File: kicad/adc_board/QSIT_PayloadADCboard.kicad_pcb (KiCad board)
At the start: 4 copper layers, 36 x 36 mm, 34 parts, among them J1 Conn_02x05_Odd_Even, J2 Conn_02x05_Odd_Even, J3 Conn_02x05_Odd_Even, U1 MCP3561_4CH, U2 NCP1117-3.3_SOT223

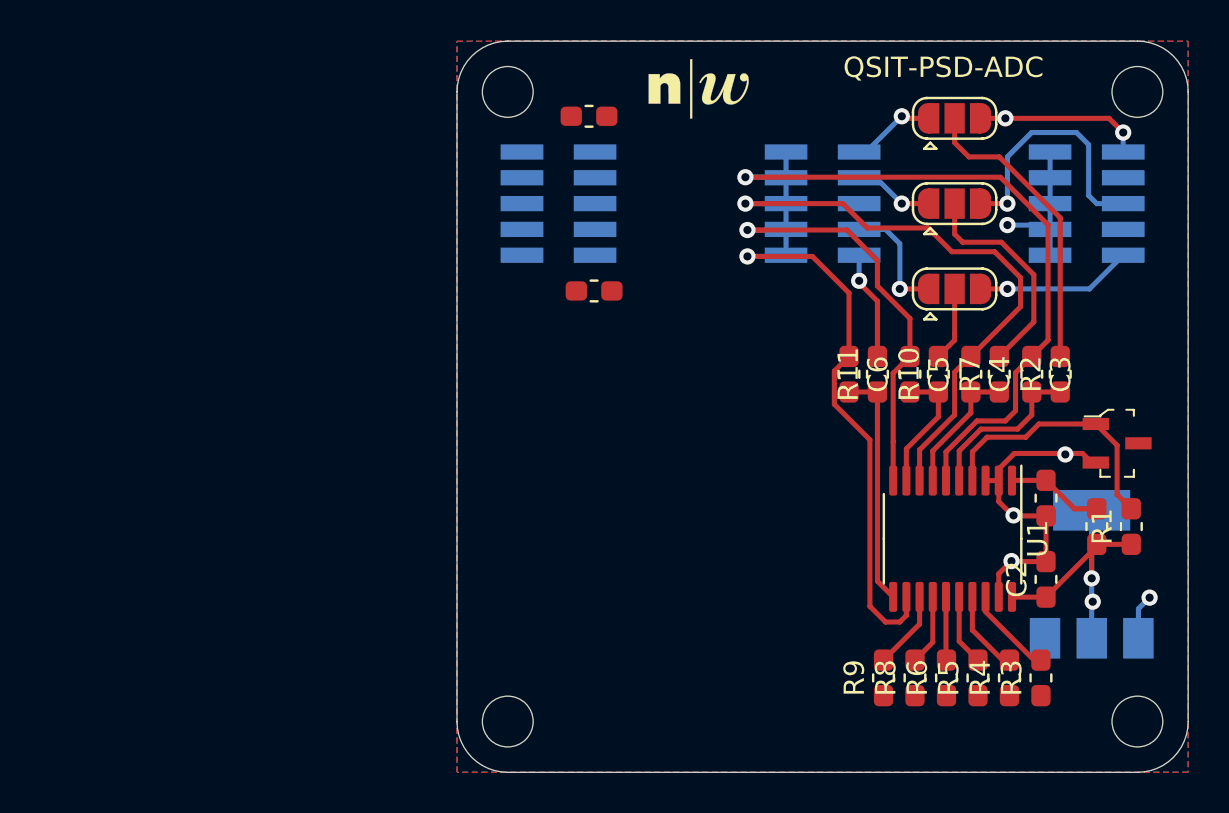
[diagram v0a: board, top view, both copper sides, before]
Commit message: changed to single 9pin connector
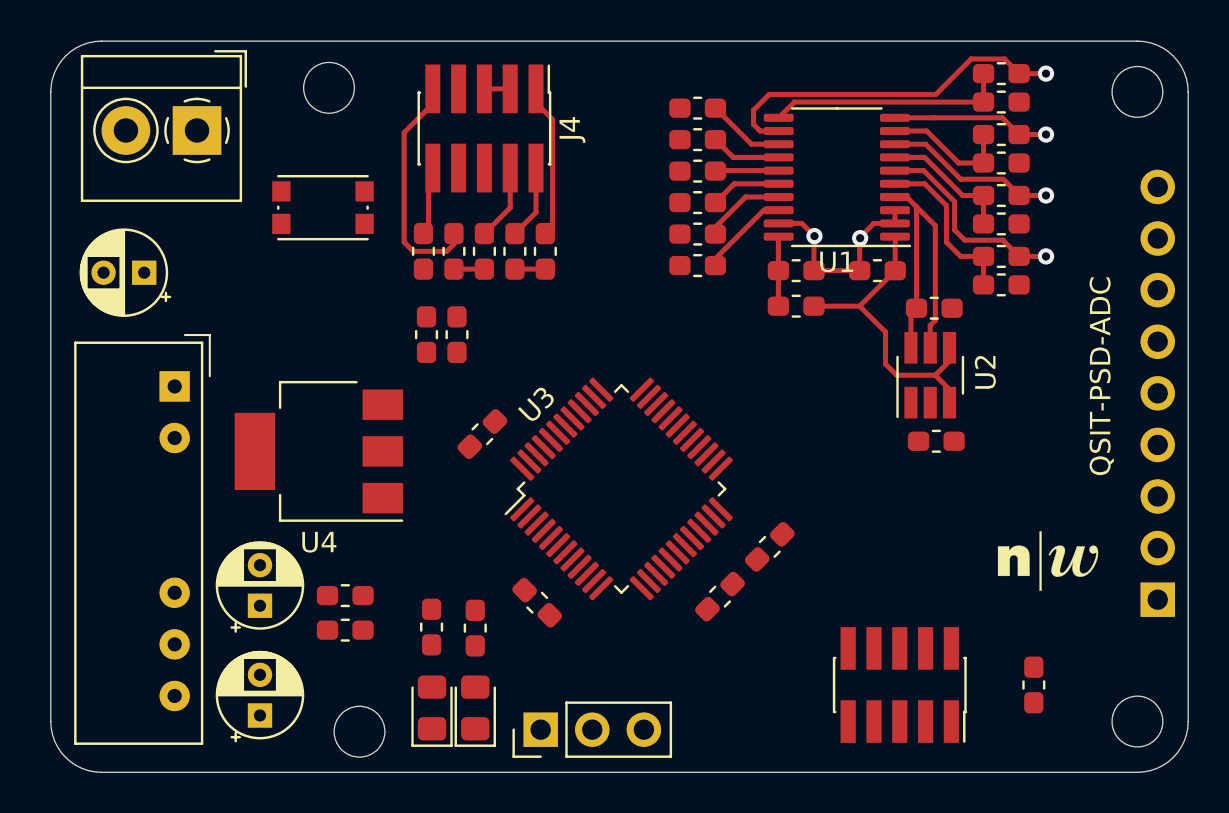
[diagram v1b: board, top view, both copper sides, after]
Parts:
- removed J3: Conn_02x05_Odd_Even, Connector_PinSocket_1.27mm:PinSocket_2x05_P1.27mm_Vertical_SMD
- removed JP1, JP2, JP3: bridge, Jumper:SolderJumper-3_P1.3mm_Open_RoundedPad1.0x1.5mm
- removed VR1: LM4040D25FTA, digikey-footprints:SOT-23-3
- added C10: 100nF, Capacitor_SMD:C_0603_1608Metric_Pad1.05x0.95mm_HandSolder, F.Cu at (135.5, 108.2)
- added C11: 100nF, Capacitor_SMD:C_0603_1608Metric_Pad1.05x0.95mm_HandSolder, F.Cu at (135.6, 114.7)
- added C12: 100nF, Capacitor_SMD:C_0603_1608Metric_Pad1.05x0.95mm_HandSolder, F.Cu at (113.2, 114.3)
- added C13: 100nF, Capacitor_SMD:C_0603_1608Metric_Pad1.05x0.95mm_HandSolder, F.Cu at (116.0, 122.7)
- added C14: 100nF, Capacitor_SMD:C_0603_1608Metric_Pad1.05x0.95mm_HandSolder, F.Cu at (127.4, 119.9)
- added C15: 100nF, Capacitor_SMD:C_0603_1608Metric_Pad1.05x0.95mm_HandSolder, F.Cu at (125.0, 122.3)
- added C16: 4u7, Capacitor_THT:CP_Radial_D4.0mm_P2.00mm, F.Cu at (102.3, 128.2)
- added C17: 2u2, Capacitor_THT:CP_Radial_D4.0mm_P2.00mm, F.Cu at (96.6, 106.4)
- added C18: 4u7, Capacitor_THT:CP_Radial_D4.0mm_P2.00mm, F.Cu at (102.3, 122.8)
- added C9: 100nF, Capacitor_SMD:C_0603_1608Metric_Pad1.05x0.95mm_HandSolder, F.Cu at (110.5, 109.5)
- added D1: LED, LED_SMD:LED_0805_2012Metric_Pad1.15x1.40mm_HandSolder, F.Cu at (110.8, 127.8)
- added D2: LED, LED_SMD:LED_0805_2012Metric_Pad1.15x1.40mm_HandSolder, F.Cu at (112.9, 127.8)
- added J4: Conn_ARM_JTAG_SWD_10, Connector_PinHeader_1.27mm:PinHeader_2x05_P1.27mm_Vertical_SMD, F.Cu at (113.3, 99.3)
- added J5: Conn_01x03, Connector_PinHeader_2.54mm:PinHeader_1x03_P2.54mm_Vertical, F.Cu at (116.1, 128.9)
- added J6: Conn_02x05_Odd_Even, Connector_PinSocket_1.27mm:PinSocket_2x05_P1.27mm_Vertical_SMD, F.Cu at (133.8, 126.7)
- added R12: 10k, Resistor_SMD:R_0603_1608Metric_Pad1.05x0.95mm_HandSolder, F.Cu at (111.8, 105.3)
- added R13: 10k, Resistor_SMD:R_0603_1608Metric_Pad1.05x0.95mm_HandSolder, F.Cu at (112.0, 109.5)
- added R14: 10R, Resistor_SMD:R_0603_1608Metric_Pad1.05x0.95mm_HandSolder, F.Cu at (113.3, 105.3)
- added R15: 10R, Resistor_SMD:R_0603_1608Metric_Pad1.05x0.95mm_HandSolder, F.Cu at (114.8, 105.3)
- added R16: 10k, Resistor_SMD:R_0603_1608Metric_Pad1.05x0.95mm_HandSolder, F.Cu at (116.3, 105.3)
- added R17: 330R, Resistor_SMD:R_0603_1608Metric_Pad1.05x0.95mm_HandSolder, F.Cu at (110.8, 123.8)
- added R18: 330R, Resistor_SMD:R_0603_1608Metric_Pad1.05x0.95mm_HandSolder, F.Cu at (112.9, 123.9)
- added R19: 10k, Resistor_SMD:R_0603_1608Metric_Pad1.05x0.95mm_HandSolder, F.Cu at (140.4, 126.7)
- added SW1: SW_Push, Button_Switch_SMD:SW_Push_1P1T_NO_CK_KMR2, F.Cu at (105.4, 103.2)
- added U3: STM32F373CCT6, Package_QFP:LQFP-48_7x7mm_P0.5mm, F.Cu at (120.1, 117.0)
- added U4: TC1108-3.3VDBTR, Package_TO_SOT_SMD:SOT-223-3_TabPin2, F.Cu at (105.2, 115.2)
- added U5: MPE1205S-1W, A_Tale_Of_A_Library:Converter_DCDC_multicorp_THT, F.Cu at (98.1, 112.0)
- J1: value Conn_02x05_Odd_Even -> Conn_01x09; footprint Connector_PinSocket_1.27mm:PinSocket_2x05_P1.27mm_Vertical_SMD -> Connector_PinHeader_2.54mm:PinHeader_1x09_P2.54mm_Vertical
- J2: value Conn_02x05_Odd_Even -> Power_Conn; footprint Connector_PinSocket_1.27mm:PinSocket_2x05_P1.27mm_Vertical_SMD -> TerminalBlock_4Ucon:TerminalBlock_4Ucon_1x02_P3.50mm_Horizontal; moved to F.Cu
- R1: value R -> 10R
- U1: value MCP3561_4CH -> MCP3564
- U2: value NCP1117-3.3_SOT223 -> MAX6070; footprint Package_TO_SOT_SMD:SOT-223-3_TabPin2 -> Package_TO_SOT_SMD:SOT-23-6_Handsoldering; moved to F.Cu
- moved J2 43.9 mm to (99.2, 99.4), turned to 180 degrees
- moved R1 37.4 mm to (110.3, 105.3)
- moved J1 35.4 mm to (146.5, 122.5)
- moved R9 29.5 mm to (123.8, 98.3), turned to 0 degrees
- moved H5 28.9 mm to (141.1, 120.6)
- moved R8 28.6 mm to (123.8, 99.8), turned to 0 degrees
- moved R6 27.8 mm to (123.8, 101.4), turned to 0 degrees
- moved R5 27.2 mm to (123.8, 103.0), turned to 0 degrees
- moved R4 26.7 mm to (123.8, 104.5), turned to 0 degrees
- moved C8 26.5 mm to (106.5, 122.3)
- moved R3 26.4 mm to (123.8, 106.0), turned to 0 degrees
- moved C7 20.7 mm to (106.5, 124.0)
- moved C2 19.6 mm to (128.7, 106.3), turned to 0 degrees
- moved U1 18.7 mm to (130.7, 101.7), turned to 180 degrees
- moved FB1 18.4 mm to (128.7, 108.0), turned to 0 degrees
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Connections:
- net Net-(R3-Pad1) renamed MCLK
- C1 pad 1: Net-(C1-Pad1) -> VAA
- FB1 pad 1: Net-(C1-Pad1) -> +3V3
- FB1 pad 2: +3V3 -> VAA
- J1 pad 1: GND -> -5V
- J1 pad 2: -5V -> GND
- J1 pad 3: GND -> +5V
- J1 pad 4: -5V -> GND
- J1 pad 5: GND -> ADC_CH1
- J1 pad 6: Net-(J1-Pad6) -> ADC_CH2
- J1 pad 7: GND -> ADC_CH3
- J1 pad 8: +5V -> ADC_CH4
- J2 pad 1: /U_signal -> +12V
- R1 pad 1: +3V3 -> ~RST
- R1 pad 2: +2V5 -> Net-(J4-Pad10)
- R10 pad 2: Net-(JP3-Pad2) -> ADC_CH3
- R11 pad 2: /X1a -> ADC_CH4
- R2 pad 2: Net-(JP1-Pad2) -> ADC_CH1
- R4 pad 1: Net-(R4-Pad1) -> SPI1_~IRQ~
- R5 pad 1: Net-(R5-Pad1) -> SPI1_MISO
- R6 pad 1: Net-(R6-Pad1) -> SPI1_MOSI
- R7 pad 2: Net-(JP2-Pad2) -> ADC_CH2
- R8 pad 1: Net-(R8-Pad1) -> SPI1_SCK
- R9 pad 1: Net-(R9-Pad1) -> SPI1_CS
- U1 pad 1: Net-(C1-Pad1) -> VAA
- U2 pad 1: GND -> Net-(C11-Pad2)
- U2 pad 2: +3V3 -> GND
- U2 pad 3: +5V -> VAA
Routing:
- net GND: track 141.5 -> 67.1 mm, vias 9 -> 6
- net VAA: track 0.00 -> 15.7 mm
- net Net-(JP1-Pad2): track 14.8 -> 0.00 mm
- net /X_signal: track 12.7 -> 0.00 mm, vias 1 -> 0
- net Net-(JP2-Pad2): track 11.0 -> 0.00 mm
- net /Y_signal: track 8.25 -> 0.00 mm, vias 2 -> 0
- net /U_signal: track 7.69 -> 0.00 mm, vias 1 -> 0
- net /Y1a: track 5.92 -> 0.00 mm, vias 1 -> 0
- net /X1a: track 5.36 -> 0.00 mm, vias 1 -> 0
- net Net-(C1-Pad1): track 4.76 -> 0.00 mm
- net /Y2a: track 4.17 -> 0.00 mm, vias 1 -> 0
- net +3V3: track 15.1 -> 11.0 mm, vias 2 -> 0
- net /X2a: track 3.93 -> 0.00 mm, vias 1 -> 0
- net Net-(J4-Pad4): track 0.00 -> 3.75 mm
- net Net-(JP3-Pad2): track 3.66 -> 0.00 mm
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- removed copper zone on B.Cu, net GND
- removed copper zone on F.Cu, net GND
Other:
- board size 36 x 36 mm -> 56 x 36 mm
- board text removed: "drawing see: UI-3242LE-NIR.pdf"

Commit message: STM32 board ready for review
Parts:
- removed R3: 10R, Resistor_SMD:R_0603_1608Metric_Pad1.05x0.95mm_HandSolder
- added C19: 12p, Capacitor_SMD:C_0603_1608Metric_Pad1.05x0.95mm_HandSolder, F.Cu at (111.6, 118.8)
- added C20: 12p, Capacitor_SMD:C_0603_1608Metric_Pad1.05x0.95mm_HandSolder, F.Cu at (111.6, 125.0)
- added R20: 10k, Resistor_SMD:R_0603_1608Metric_Pad1.05x0.95mm_HandSolder, F.Cu at (107.0, 102.0)
- added TP1: TestPoint, TestPoint:TestPoint_Keystone_5000-5004_Miniature, F.Cu at (106.2, 105.5)
- added X1: ECS-2520MVLC-049-BN, Oscillator:Oscillator_SMD_ECS_2520MV-xxx-xx-4Pin_2.5x2.0mm, F.Cu at (127.0, 110.9)
- added Y1: Crystal_GND24, Crystal:Crystal_SMD_TXC_7M-4Pin_3.2x2.5mm, F.Cu at (111.6, 121.9)
- moved D2 28.3 mm to (102.5, 101.6), turned to 270 degrees
- moved D1 27.0 mm to (104.6, 101.6), turned to 270 degrees
- moved R18 20.6 mm to (102.0, 106.4), turned to 90 degrees
- moved R17 18.9 mm to (103.6, 106.4), turned to 90 degrees
- moved R19 12.2 mm to (128.2, 126.7), turned to 270 degrees
- moved R6 6.29 mm to (121.3, 107.2), turned to 90 degrees
- moved H5 6.17 mm to (142.0, 114.5), turned to 90 degrees
- moved SW1 4.71 mm to (109.8, 105.0), turned to 270 degrees
- moved R5 4.32 mm to (122.8, 107.2), turned to 90 degrees
- moved J5 3.65 mm to (119.7, 128.2)
- moved R4 2.71 mm to (124.4, 107.2), turned to 90 degrees
- moved J4 2.30 mm to (115.7, 99.4)
- moved R1 2.30 mm to (112.7, 105.5)
- moved R12 2.30 mm to (114.2, 105.5)
- moved R14 2.30 mm to (115.7, 105.5)
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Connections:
- net BOOT1 renamed Net-(U3-Pad20)
- U1 pad 18: Net-(R3-Pad2) -> MCLK
- U3 pad 29: Net-(U3-Pad29) -> MEMS_OUT_EN
- U3 pad 31: TIM14_CH1 -> FCLK_X
- U3 pad 33: TIM16_CH1 -> FCLK_Y
- U3 pad 44: Net-(U3-Pad44) -> BOOT0
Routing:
- net +3V3: track 11.0 -> 104.4 mm, vias 0 -> 6
- net +5V: track 0.00 -> 87.6 mm, vias 0 -> 1
- net GND: track 67.1 -> 128.2 mm, vias 6 -> 18
- net -5V: track 0.00 -> 59.8 mm
- net SPI1_CS: track 0.00 -> 29.5 mm, vias 0 -> 2
- net SPI1_SCK: track 0.00 -> 29.5 mm, vias 0 -> 2
- net ~RST: track 0.00 -> 28.0 mm, vias 0 -> 2
- net FCLK_Y: track 0.00 -> 26.1 mm
- net SPI2_SCK: track 0.00 -> 25.6 mm, vias 0 -> 2
- net MEMS_OUT_EN: track 0.00 -> 25.5 mm
- net SPI2_MOSI: track 0.00 -> 24.1 mm, vias 0 -> 2
- net FCLK_X: track 0.00 -> 19.9 mm
- net SPI1_MISO: track 0.00 -> 19.6 mm, vias 0 -> 2
- net BOOT0: track 0.00 -> 18.4 mm, vias 0 -> 1
- net SPI2_CS: track 0.00 -> 16.9 mm
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- added copper zone on B.Cu, net (none)
- added copper zone on F.Cu, net +3V3
- added copper zone on F.Cu, net GND
- added copper zone on In2.Cu, net GND
- removed copper zone on In2.Cu, net (none)
- removed copper zone on In1.Cu, net GND
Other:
- net class power: via_dia 0.8 -> 1; via_drill 0.4 -> 0.6
- board text added: "+12V"
- board text added: "MEMS"
- board text added: "PSD"
- board text added: "SWD"

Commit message: further pcb improvements
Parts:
- added C21: 4u7, Capacitor_SMD:C_1206_3216Metric, F.Cu at (110.0, 113.2)
- added C22: 100nF, Capacitor_SMD:C_0603_1608Metric, F.Cu at (138.0, 112.0)
- C16, C18: footprint Capacitor_THT:CP_Radial_D4.0mm_P2.00mm -> Capacitor_SMD:C_1206_3216Metric
- U5: footprint A_Tale_Of_A_Library:Converter_DCDC_multicorp_THT -> simonmartin_kicad_lib:Converter_DCDC_multicorp_THT
- moved H5 31.3 mm to (114.0, 128.5), turned to 0 degrees
- moved C7 3.59 mm to (103.7, 127.5), turned to 270 degrees
- moved C8 2.82 mm to (103.7, 121.5), turned to 270 degrees
- moved C16 1.44 mm to (101.5, 127.0), turned to 270 degrees
- moved C18 1.13 mm to (101.5, 122.0), turned to 270 degrees
- moved U4 0.45 mm to (104.3, 114.5)
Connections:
- C16 pad 1: +5V -> GND
- C16 pad 2: GND -> +5V
- C18 pad 1: GND -> -5V
- C18 pad 2: -5V -> GND
- J5 pad 1: USART2_TX -> GND
- J5 pad 3: GND -> USART2_TX
- U3 pad 42: Net-(U3-Pad42) -> LED2
- U3 pad 43: Net-(U3-Pad43) -> LED1
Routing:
- net LED2: track 0.00 -> 25.1 mm, vias 0 -> 2
- net LED1: track 0.00 -> 21.1 mm, vias 0 -> 2
- net +5V: track 87.6 -> 81.0 mm
- net -5V: track 59.8 -> 55.7 mm
- net GND: track 128.2 -> 132.0 mm, vias 18 -> 44
- net +3V3: track 104.4 -> 107.2 mm
- net VAA: track 16.1 -> 17.9 mm
- added copper zone on B.Cu, net GND
- added copper zone on In1.GND, net GND
- removed copper zone on B.Cu, net (none)
- removed copper zone on In2.Cu, net GND
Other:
- board text added: "11-13V"
- board text added: "In.Layer tauschen GND vs. Vcc"
- board text added: "RST"
- board text added: "check pinout!"
- board text added: "rev 1.0"
- board text added: "wrong pin order on MEMS connector !!"
- board text removed: "+12V"

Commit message: rev.1 of ADC board
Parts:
- J5: value Conn_01x03 -> UART
- J6: footprint Connector_PinSocket_1.27mm:PinSocket_2x05_P1.27mm_Vertical_SMD -> Connector_PinHeader_1.27mm:PinHeader_2x05_P1.27mm_Vertical_SMD
- Y1: value Crystal_GND24 -> 8MHz
- moved J5 4.54 mm to (124.2, 128.0), turned to 270 degrees
- moved R19 1.12 mm to (127.3, 126.1)
- moved X1 0.30 mm to (127.0, 110.6)
- moved J6 0.10 mm to (134.9, 126.2), turned to 270 degrees
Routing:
- net +5V: track 81.0 -> 85.9 mm, vias 1 -> 2
- net LED1: track 21.1 -> 25.2 mm
- net -5V: track 55.7 -> 59.3 mm
- net LED2: track 25.1 -> 28.6 mm
- net SPI2_CS: track 16.9 -> 13.9 mm
- net FCLK_Y: track 26.1 -> 28.4 mm, vias 0 -> 2
- net GND: track 132.0 -> 134.3 mm, vias 44 -> 42
- net FCLK_X: track 19.9 -> 18.8 mm, vias 0 -> 2
- net MEMS_OUT_EN: track 25.5 -> 26.3 mm
- net SPI2_MOSI: track 24.1 -> 23.4 mm
- net SPI2_SCK: track 25.6 -> 25.1 mm
- net +3V3: track 107.2 -> 107.4 mm, vias 6 -> 10
- added copper zone on In2.Vcc, net (none)
- added copper zone on In2.Vcc, net +3V3
- added copper zone on In2.Vcc, net +5V
- added copper zone on In2.Vcc, net -5V
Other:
- board text removed: "In.Layer tauschen GND vs. Vcc"
- board text removed: "check pinout!"
- board text removed: "wrong pin order on MEMS connector !!"

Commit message: rev 1 finished - final check on PSD frontend - plotted gerbber for jlc - added simulation for PSD frontend
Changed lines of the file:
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@@
     (35 F.Paste user hide)
     (36 B.SilkS user)
-    (37 F.SilkS user)
+    (37 F.SilkS user hide)
     (38 B.Mask user hide)
     (39 F.Mask user hide)
-    (40 Dwgs.User user)
+    (40 Dwgs.User user hide)
     (41 Cmts.User user hide)
     (42 Eco1.User user hide)
@@
     (45 Margin user hide)
     (46 B.CrtYd user hide)
-    (47 F.CrtYd user)
+    (47 F.CrtYd user hide)
     (48 B.Fab user hide)
-    (49 F.Fab user)
+    (49 F.Fab user hide)
   )
   (setup
@@
     (pcbplotparams
       (layerselection 0x010fc_ffffffff)
-      (usegerberextensions false)
+      (usegerberextensions true)
       (usegerberattributes true)
       (usegerberadvancedattributes true)
@@
       (psa4output false)
       (plotreference true)
-      (plotvalue true)
+      (plotvalue false)
       (plotinvisibletext false)
       (padsonsilk false)
-      (subtractmaskfromsilk false)
+      (subtractmaskfromsilk true)
       (outputformat 1)
       (mirror false)
-      (drillshape 1)
+      (drillshape 0)
       (scaleselection 1)
-      (outputdirectory ""))
+      (outputdirectory "../../gerber/ADC rev 1/"))
   )
   (net 0 "")
@@
       (effects (font (size 0.5 0.5) (thickness 0.08)))
     )
-    (pad 2 smd roundrect (at 1.025 0 270) (size 1.15 1.4) (layers F.Cu F.Paste F.Mask) (roundrect_rratio 0.217391)
+    (pad 2 smd roundrect (at 1.025 0 270) (size 1.15 1.4) (layers F.Cu F.Paste F.Mask) (roundrect_rratio 0.2173904347826087)
       (net 21 "Net-(D1-Pad2)"))
-    (pad 1 smd roundrect (at -1.025 0 270) (size 1.15 1.4) (layers F.Cu F.Paste F.Mask) (roundrect_rratio 0.217391)
+    (pad 1 smd roundrect (at -1.025 0 270) (size 1.15 1.4) (layers F.Cu F.Paste F.Mask) (roundrect_rratio 0.2173904347826087)
       (net 2 GND))
     (model ${KISYS3DMOD}/LED_SMD.3dshapes/LED_0805_2012Metric.wrl
@@
       (effects (font (size 0.5 0.5) (thickness 0.08)))
     )
-    (pad 1 smd roundrect (at -1.025 0 270) (size 1.15 1.4) (layers F.Cu F.Paste F.Mask) (roundrect_rratio 0.217391)
+    (pad 1 smd roundrect (at -1.025 0 270) (size 1.15 1.4) (layers F.Cu F.Paste F.Mask) (roundrect_rratio 0.2173904347826087)
       (net 2 GND))
-    (pad 2 smd roundrect (at 1.025 0 270) (size 1.15 1.4) (layers F.Cu F.Paste F.Mask) (roundrect_rratio 0.217391)
+    (pad 2 smd roundrect (at 1.025 0 270) (size 1.15 1.4) (layers F.Cu F.Paste F.Mask) (roundrect_rratio 0.2173904347826087)
       (net 22 "Net-(D2-Pad2)"))
     (model ${KISYS3DMOD}/LED_SMD.3dshapes/LED_0805_2012Metric.wrl
@@
       (effects (font (size 0.8 0.8) (thickness 0.12)))
     )
-    (pad 1 smd roundrect (at -1.475 0 90) (size 1.15 1.8) (layers F.Cu F.Paste F.Mask) (roundrect_rratio 0.217391)
+    (pad 1 smd roundrect (at -1.475 0 90) (size 1.15 1.8) (layers F.Cu F.Paste F.Mask) (roundrect_rratio 0.2173904347826087)
       (net 2 GND))
-    (pad 2 smd roundrect (at 1.475 0 90) (size 1.15 1.8) (layers F.Cu F.Paste F.Mask) (roundrect_rratio 0.217391)
+    (pad 2 smd roundrect (at 1.475 0 90) (size 1.15 1.8) (layers F.Cu F.Paste F.Mask) (roundrect_rratio 0.2173904347826087)
       (net 9 +3V3))
     (model ${KISYS3DMOD}/Capacitor_SMD.3dshapes/C_1206_3216Metric.wrl
@@
   (gr_line (start 148 97.5) (end 148 128.5) (layer Edge.Cuts) (width 0.05))
   (gr_line (start 94.5 95) (end 145.5 95) (layer Edge.Cuts) (width 0.05))
-  (via (at 103.5 110.75) (size 0.8) (drill 0.4) (layers F.Cu B.Cu) (net 9))
-  (via (at 103.5 112.5) (size 0.8) (drill 0.4) (layers F.Cu B.Cu) (net 9))
-  (via (at 104.85 110.75) (size 0.8) (drill 0.4) (layers F.Cu B.Cu) (net 9))
-  (via (at 104.85 112.5) (size 0.8) (drill 0.4) (layers F.Cu B.Cu) (net 9))
-  (via (at 129.3 126.3) (size 0.8) (drill 0.4) (layers F.Cu B.Cu) (net 3) (status 40000))
   (segment (start 124.85 100.725) (end 124.225 101.35) (width 0.25) (layer F.Cu) (net 1))
   (segment (start 127.8375 100.725) (end 124.85 100.725) (width 0.25) (layer F.Cu) (net 1))
@@
   (segment (start 128.875 109.675) (end 129.175 109.975) (width 0.5) (layer F.Cu) (net 2))
   (segment (start 127.725 109.675) (end 128.875 109.675) (width 0.5) (layer F.Cu) (net 2))
+  (via (at 129.3 126.3) (size 0.8) (drill 0.4) (layers F.Cu B.Cu) (net 3) (status 40000))
   (via (at 130.5 126.3) (size 0.8) (drill 0.4) (layers F.Cu B.Cu) (net 3))
   (segment (start 130.5 128.3) (end 130.5 126.3) (width 1) (layer F.Cu) (net 3))
@@
   (segment (start 141.05 127.95) (end 127.85 127.95) (width 1) (layer In2.Vcc) (net 4))
   (segment (start 146.5 122.5) (end 141.05 127.95) (width 1) (layer In2.Vcc) (net 4))
+  (via (at 103.5 110.75) (size 0.8) (drill 0.4) (layers F.Cu B.Cu) (net 9))
+  (via (at 103.5 112.5) (size 0.8) (drill 0.4) (layers F.Cu B.Cu) (net 9))
+  (via (at 104.85 110.75) (size 0.8) (drill 0.4) (layers F.Cu B.Cu) (net 9))
+  (via (at 104.85 112.5) (size 0.8) (drill 0.4) (layers F.Cu B.Cu) (net 9))
   (segment (start 118.19 98.14) (end 118.19 97.45) (width 0.25) (layer F.Cu) (net 9))
   (segment (start 118.65 104.575) (end 119 104.225) (width 0.5) (layer F.Cu) (net 9))
